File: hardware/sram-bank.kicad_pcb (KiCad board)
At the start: 2 copper layers, 50.8 x 78.7 mm, 42 parts, among them U1 74LVC138A, U10 74LVC8T245, U11 74LVC8T245, U12 IS66WV51216EALL, U13 74LVC138A, U2 74LVC8T245, U3 74LVC8T245, U4 74LVC8T245, U5 74LVC8T245, U6 74LVC8T245, U7 74LVC8T245, U8 74LVC8T245, U9 74LVC8T245

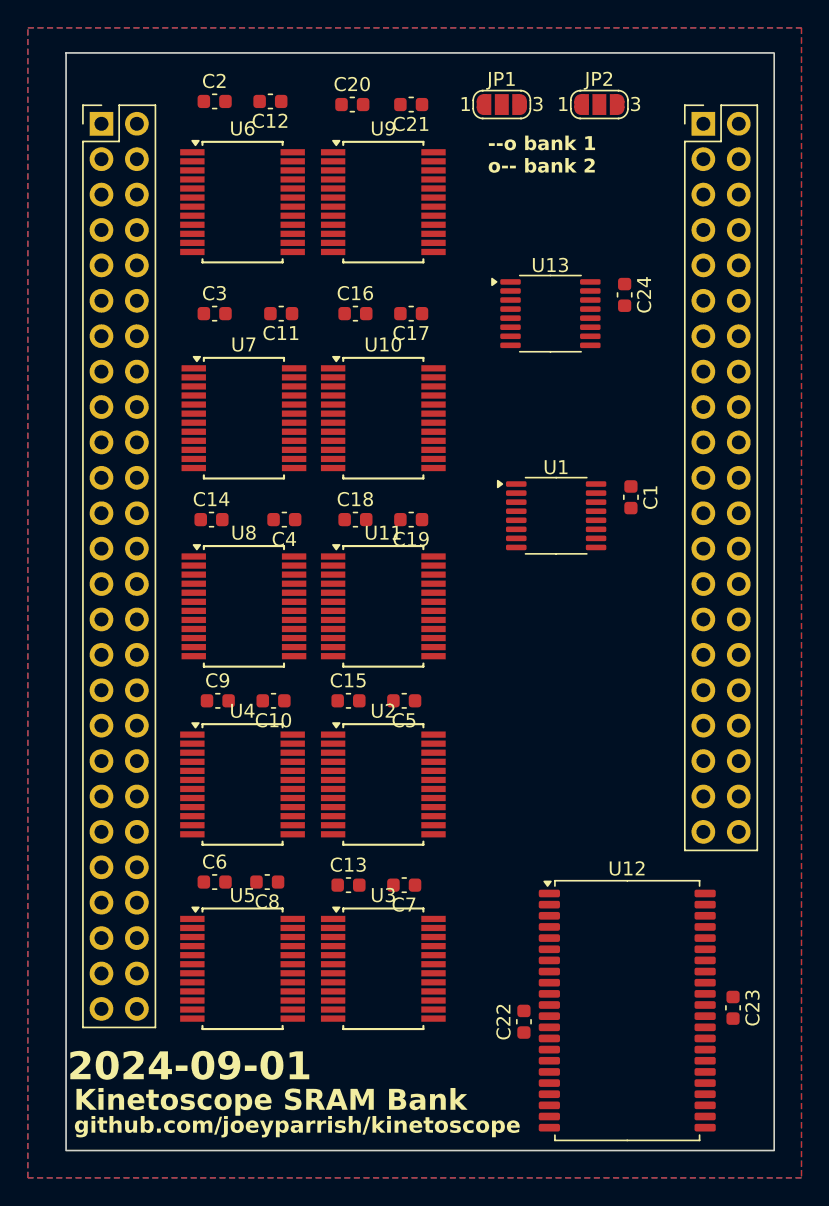
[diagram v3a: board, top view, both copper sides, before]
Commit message: Add test pads to SRAM board
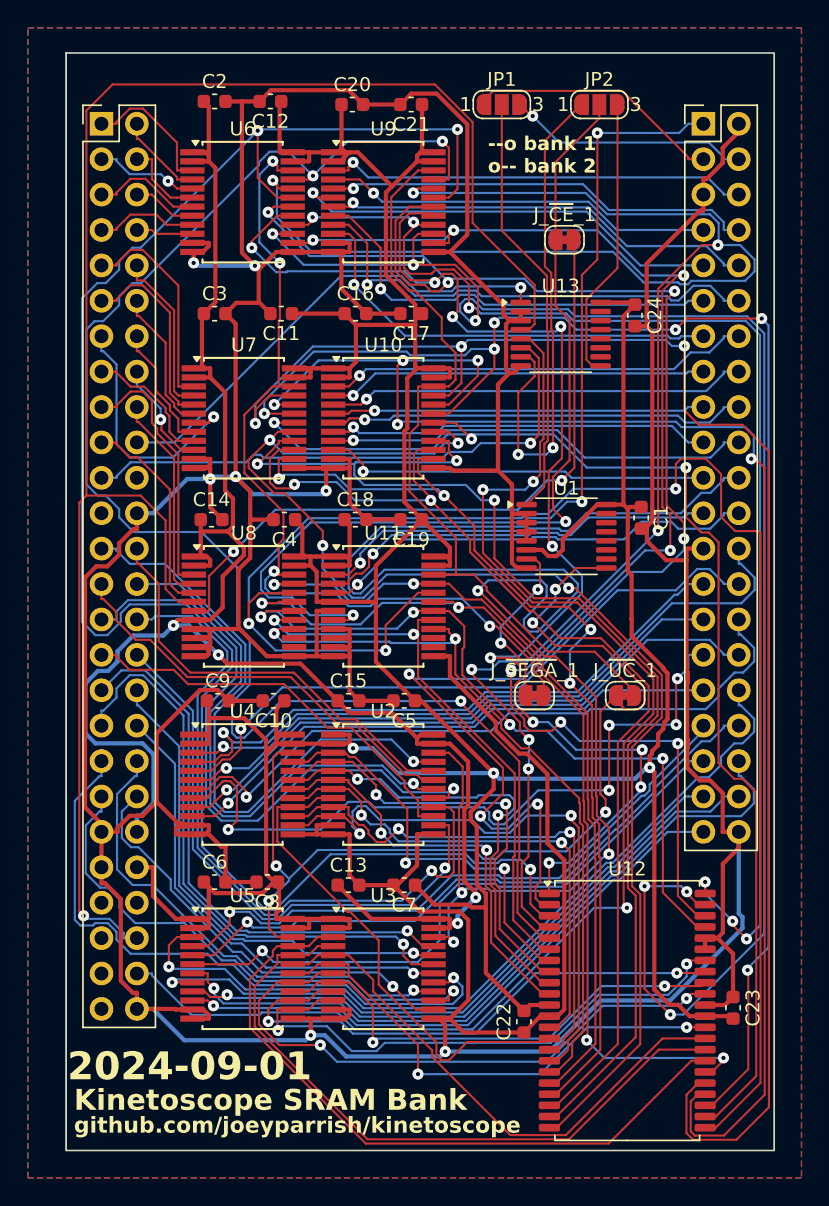
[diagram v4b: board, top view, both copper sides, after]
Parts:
- added J_~{CE}_1: ~, Jumper:SolderJumper-2_P1.3mm_Bridged_RoundedPad1.0x1.5mm, F.Cu at (54.5, 32.7)
- added J_~{SEGA}_1: ~, Jumper:SolderJumper-2_P1.3mm_Bridged_RoundedPad1.0x1.5mm, F.Cu at (52.4, 65.4)
- added J_~{UC}_1: ~, Jumper:SolderJumper-2_P1.3mm_Bridged_RoundedPad1.0x1.5mm, F.Cu at (58.9, 65.4)
- moved U1 1.65 mm to (54.6, 54.0)
- moved U13 1.65 mm to (54.2, 39.5)
- moved C1 1.65 mm to (60.0, 52.6)
- moved C24 1.65 mm to (59.5, 38.1)
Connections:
- U10 pad 22: /~{UC_CONTROL} -> /~{UC_CONTROL_INT}
- U11 pad 22: /~{UC_CONTROL} -> /~{UC_CONTROL_INT}
- U6 pad 22: /~{SEGA_CONTROL} -> /~{SEGA_CONTROL_INT}
- U7 pad 22: /~{SEGA_CONTROL} -> /~{SEGA_CONTROL_INT}
- U8 pad 22: /~{SEGA_CONTROL} -> /~{SEGA_CONTROL_INT}
- U8 pad 7: /~{SRAM_CE} -> /~{SRAM_CE_INT}
- U9 pad 22: /~{UC_CONTROL} -> /~{UC_CONTROL_INT}
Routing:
- net GND: track 0.00 -> 503.0 mm, vias 0 -> 7
- net +3.3V: track 0.00 -> 314.0 mm, vias 0 -> 3
- net /~{SRAM_CE}: track 0.00 -> 136.3 mm, vias 0 -> 5
- net /SRAM_A1: track 0.00 -> 133.1 mm, vias 0 -> 7
- net +5V: track 0.00 -> 129.9 mm, vias 0 -> 4
- net /SRAM_A2: track 0.00 -> 129.0 mm, vias 0 -> 3
- net /~{SEGA_CE}: track 0.00 -> 123.6 mm, vias 0 -> 1
- net /SRAM_A17: track 0.00 -> 115.7 mm, vias 0 -> 3
- net /SRAM_A6: track 0.00 -> 115.7 mm, vias 0 -> 6
- net /SRAM_A3: track 0.00 -> 115.2 mm, vias 0 -> 7
- net /SRAM_A8: track 0.00 -> 113.9 mm, vias 0 -> 3
- net /SRAM_A0: track 0.00 -> 113.8 mm, vias 0 -> 3
- net /SRAM_A9: track 0.00 -> 111.3 mm, vias 0 -> 5
- net /SRAM_A10: track 0.00 -> 109.2 mm, vias 0 -> 6
- net /SRAM_A4: track 0.00 -> 99.3 mm, vias 0 -> 10
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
